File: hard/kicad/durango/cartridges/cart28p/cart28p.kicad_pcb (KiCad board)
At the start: 2 copper layers, 6 parts, among them J2 CARTRIDGE SLOT, U1 27C512

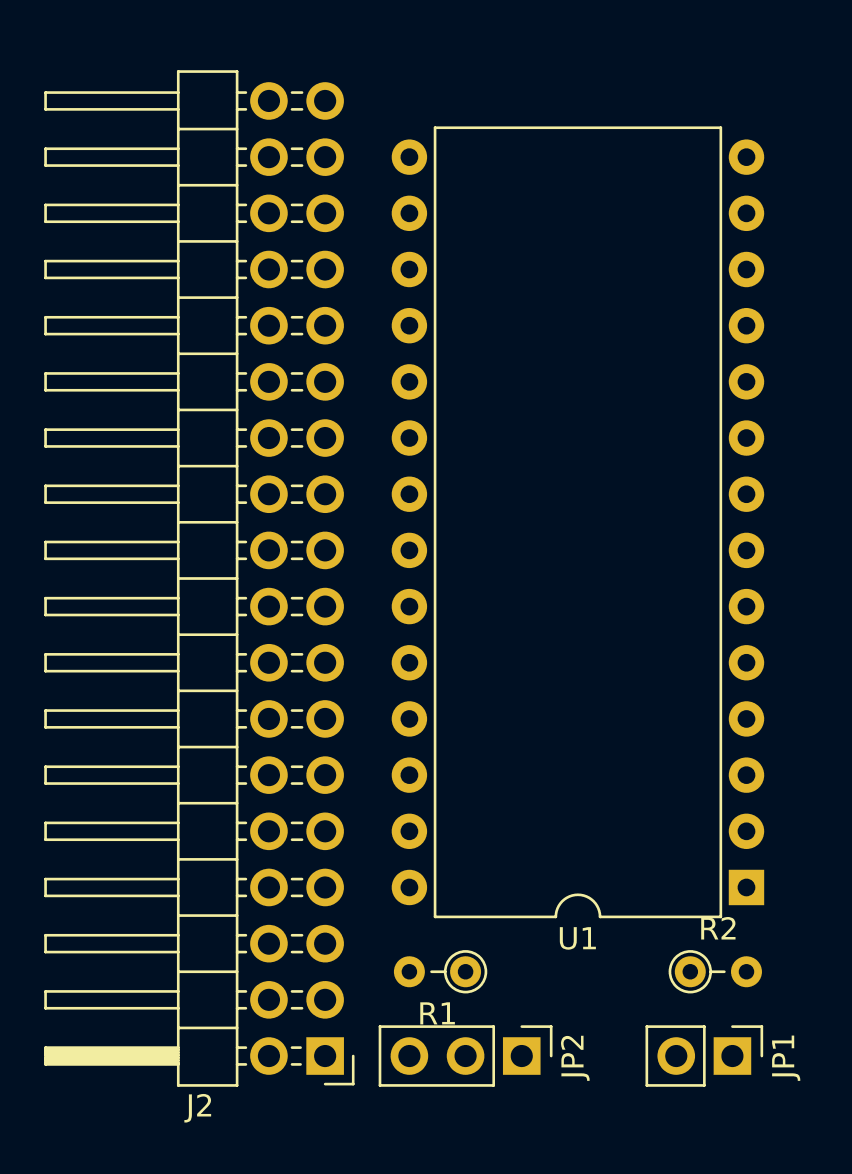
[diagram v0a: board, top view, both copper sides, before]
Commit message: fill 28p cartridge
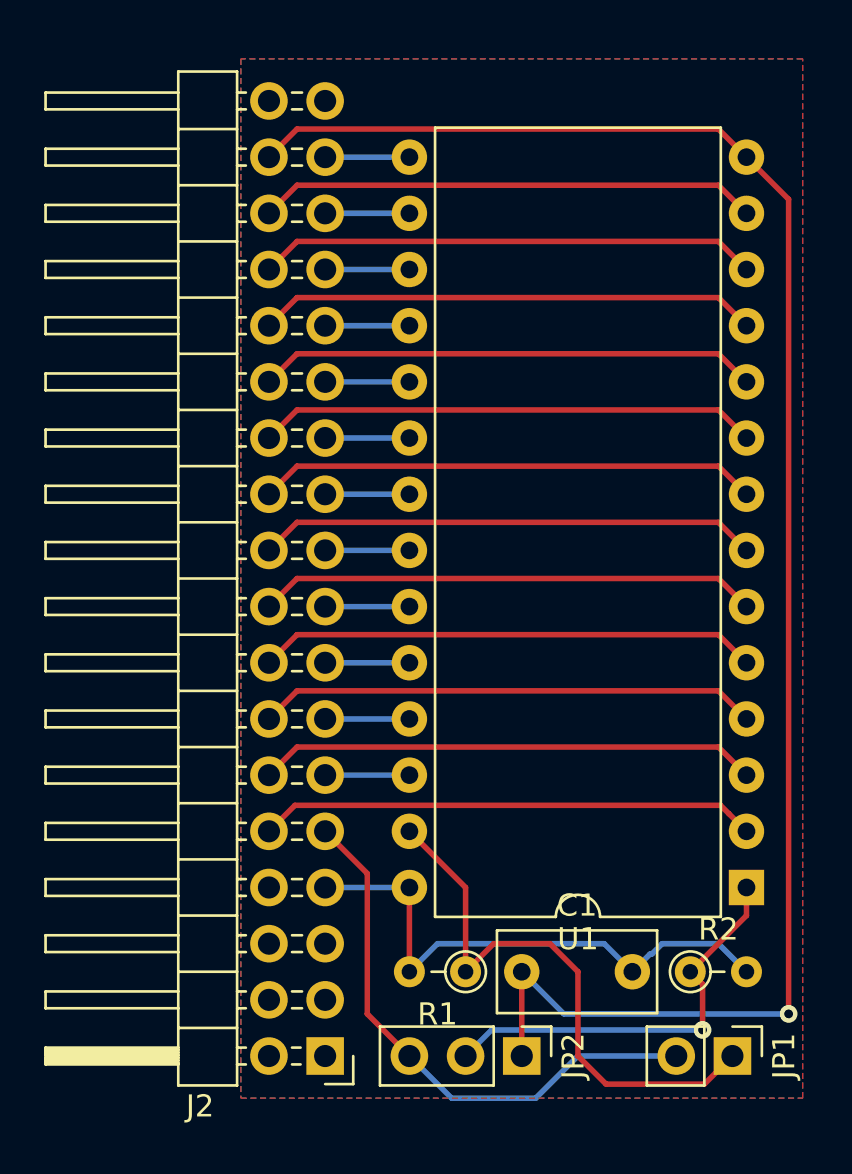
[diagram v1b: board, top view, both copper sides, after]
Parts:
- added C1: 100n, Capacitor_THT:C_Rect_L7.0mm_W3.5mm_P5.00mm, F.Cu at (71.8, 69.8)
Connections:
- net Net-(JP1-Pad1) renamed /A14_32+
- net Net-(JP2-Pad2) renamed /A15_F
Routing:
- net GND: track 0.00 -> 78.8 mm, vias 0 -> 1
- net /A14_32+: track 0.00 -> 25.4 mm
- net /A14: track 0.00 -> 25.4 mm
- net +5V: track 0.00 -> 25.0 mm
- net /D2: track 0.00 -> 22.6 mm
- net /D1: track 0.00 -> 22.6 mm
- net /D0: track 0.00 -> 22.6 mm
- net /A7: track 0.00 -> 22.6 mm
- net /A6: track 0.00 -> 22.6 mm
- net /A5: track 0.00 -> 22.6 mm
- net /A4: track 0.00 -> 22.6 mm
- net /A0: track 0.00 -> 22.6 mm
- net /A3: track 0.00 -> 22.6 mm
- net /A2: track 0.00 -> 22.6 mm
- net /A1: track 0.00 -> 22.6 mm
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- added copper zone on B.Cu, net +5V
- added copper zone on F.Cu, net GND

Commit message: add cartridge edge connector
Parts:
- removed J2: CARTRIDGE SLOT, Connector_PinHeader_2.54mm:PinHeader_2x18_P2.54mm_Horizontal
- added J1: Edge Connector, edge_conn:Durango_ROM, F.Cu at (55.9, 27.9)
- moved R2 2.54 mm to (81.9, 69.8), turned to 180 degrees
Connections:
- net /A15_F renamed /A15
- JP1 pad 1: /A14_32+ -> /A14
- JP1 pad 2: /A14 -> /CA14
- JP2 pad 3: /A14 -> /CA14
- R1 pad 1: /A14_32+ -> /A14
- U1 pad 27: /A14_32+ -> /A14
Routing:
- net /CA14: track 0.00 -> 31.3 mm
- net /A14_32+: track 25.4 -> 0.00 mm
- net GND: track 78.8 -> 73.3 mm, vias 1 -> 0
- net /~OE: track 3.81 -> 6.98 mm
- net /~CS: track 3.81 -> 6.98 mm
- net /D7: track 3.81 -> 6.98 mm
- net /D6: track 3.81 -> 6.98 mm
- net /D5: track 3.81 -> 6.98 mm
- net /D4: track 3.81 -> 6.98 mm
- net /D3: track 3.81 -> 6.98 mm
- net /A9: track 3.81 -> 6.98 mm
- net /A8: track 3.81 -> 6.98 mm
- net /A13: track 3.81 -> 6.98 mm
- net /A11: track 3.81 -> 6.98 mm
- net /A10: track 3.81 -> 6.98 mm
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- added copper zone on F.Cu, net +5V
- added copper zone on B.Cu, net GND
- removed copper zone on B.Cu, net +5V
- removed copper zone on F.Cu, net GND
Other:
- board outline added: 27.9 x 48.3 mm
- net class POWER added: clearance 0.25, trace_width 0.4, via_dia 0.8, via_drill 0.4

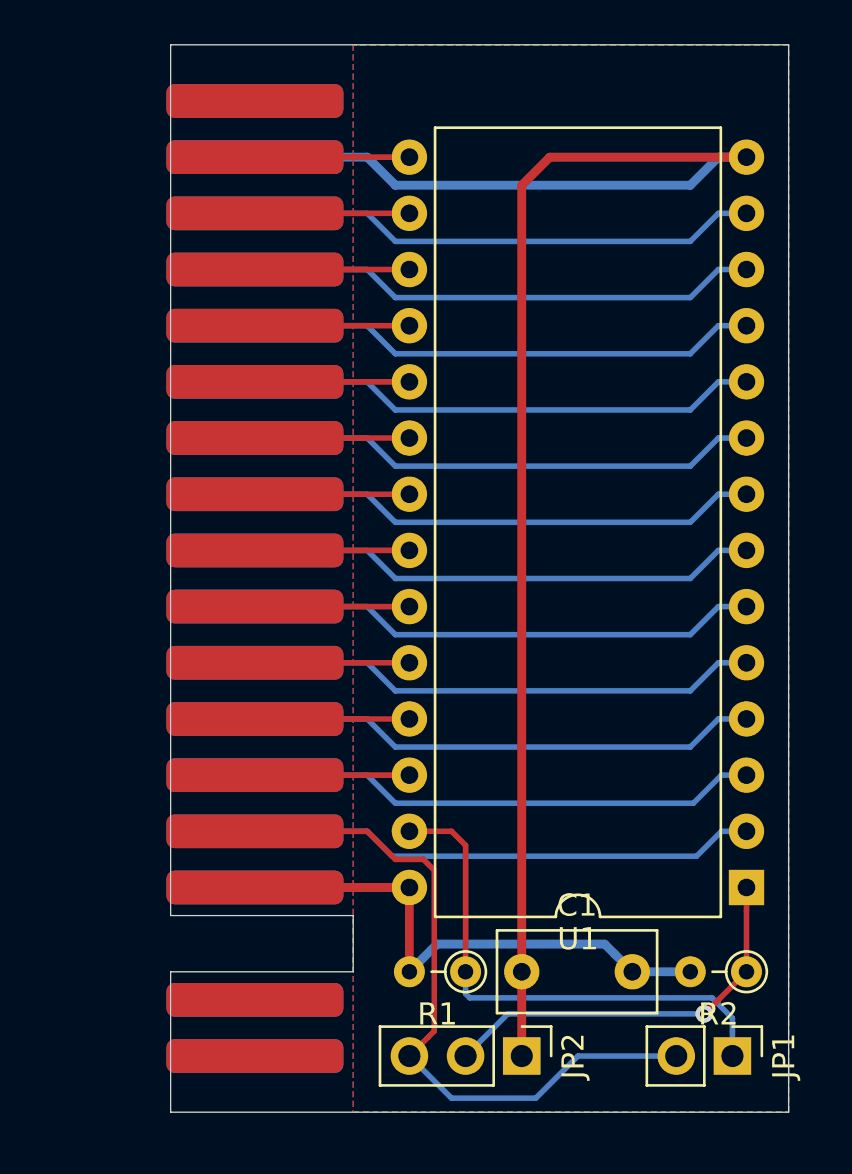
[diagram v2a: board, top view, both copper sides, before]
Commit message: improve 28p cartridge design
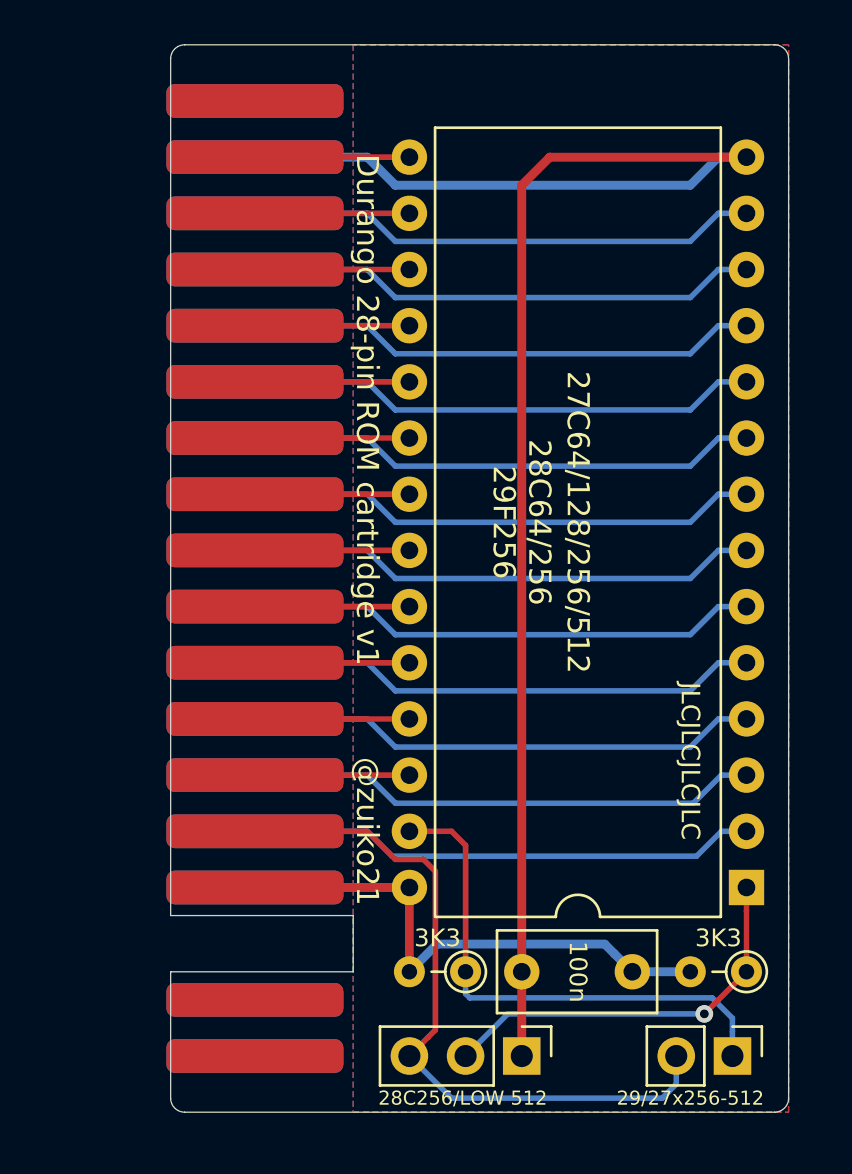
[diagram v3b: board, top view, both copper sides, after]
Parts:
- JP1: value 27x256-512 -> 29/27x256-512
- JP2: value LOW 512/28C256 -> 28C256/LOW 512
- U1: value 27C512 -> 27C64/128/256/512
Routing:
- net /CA14: track 31.3 -> 32.1 mm
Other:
- outline, holes or cut-outs redrawn
- board text added: "28C64/256 29F256"
- board text added: "@zuiko21"
- board text added: "Durango 28-pin ROM cartridge v1"
- board text added: "JLCJLCJLCJLC"

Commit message: add wrong gerbers for 28p cart
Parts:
- JP1: value 29/27x256-512 -> 27/29-32K+
- JP2: value 28C256/LOW 512 -> 28C/L32
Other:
- outline, holes or cut-outs redrawn
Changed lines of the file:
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@@
   (general
     (thickness 1.6)
-    (drawings 17)
+    (drawings 16)
     (tracks 115)
     (zones 0)
@@
   (page A4)
   (layers
-    (0 F.Cu signal)
-    (31 B.Cu signal)
-    (32 B.Adhes user)
-    (33 F.Adhes user)
-    (34 B.Paste user)
-    (35 F.Paste user)
-    (36 B.SilkS user)
-    (37 F.SilkS user)
-    (38 B.Mask user)
-    (39 F.Mask user)
-    (40 Dwgs.User user)
-    (41 Cmts.User user)
-    (42 Eco1.User user)
-    (43 Eco2.User user)
+    (0 F.Cu signal hide)
+    (31 B.Cu signal hide)
+    (32 B.Adhes user hide)
+    (33 F.Adhes user hide)
+    (34 B.Paste user hide)
+    (35 F.Paste user hide)
+    (36 B.SilkS user hide)
+    (37 F.SilkS user hide)
+    (38 B.Mask user hide)
+    (39 F.Mask user hide)
+    (40 Dwgs.User user hide)
+    (41 Cmts.User user hide)
+    (42 Eco1.User user hide)
+    (43 Eco2.User user hide)
     (44 Edge.Cuts user)
-    (45 Margin user)
-    (46 B.CrtYd user)
-    (47 F.CrtYd user)
-    (48 B.Fab user)
-    (49 F.Fab user)
+    (45 Margin user hide)
+    (46 B.CrtYd user hide)
+    (47 F.CrtYd user hide)
+    (48 B.Fab user hide)
+    (49 F.Fab user hide)
   )
   (setup
@@
     (pcbplotparams
       (layerselection 0x010fc_ffffffff)
-      (usegerberextensions false)
+      (usegerberextensions true)
       (usegerberattributes false)
       (usegerberadvancedattributes false)
       (creategerberjobfile false)
       (excludeedgelayer true)
-      (linewidth 0.100000)
+      (linewidth 0.150000)
       (plotframeref false)
       (viasonmask false)
@@
       (plotinvisibletext false)
       (padsonsilk false)
-      (subtractmaskfromsilk false)
+      (subtractmaskfromsilk true)
       (outputformat 1)
       (mirror false)
-      (drillshape 1)
+      (drillshape 0)
       (scaleselection 1)
-      (outputdirectory ""))
+      (outputdirectory "gerber/"))
   )
   (net 0 "")
@@
     (at 55.88 27.94 270)
     (fp_text reference J1 (at 2.54 -8.89 unlocked) (layer B.SilkS)
-      (effects (font (size 1 1) (thickness 0.15)) (justify mirror))
+      (effects (font (size 1.016 1.016) (thickness 0.16)) (justify mirror))
     )
     (fp_text value "Edge Connector" (at 24.13 1.27 90) (layer F.Fab)
@@
     (tags "THT DIP DIL PDIP 2.54mm 15.24mm 600mil")
     (fp_text reference U1 (at 7.493 16.51 unlocked) (layer B.SilkS)
-      (effects (font (size 1 1) (thickness 0.15)) (justify mirror))
+      (effects (font (size 1.016 1.016) (thickness 0.16)) (justify mirror))
     )
     (fp_text value 27C64/128/256/512 (at 7.62 16.51 270 unlocked) (layer F.SilkS)
-      (effects (font (size 1 1) (thickness 0.15)))
+      (effects (font (size 1.016 1.016) (thickness 0.16)))
     )
     (fp_arc (start 7.62 -1.33) (end 6.62 -1.33) (angle -180) (layer F.SilkS) (width 0.12))
@@
     (tags "C Rect series Radial pin pitch 5.00mm  length 7mm width 3.5mm Capacitor")
     (fp_text reference C1 (at 2.5 0) (layer B.SilkS)
-      (effects (font (size 1 1) (thickness 0.15)) (justify mirror))
+      (effects (font (size 1 1) (thickness 0.16)) (justify mirror))
     )
     (fp_text value 100n (at 2.54 0 270 unlocked) (layer F.SilkS)
-      (effects (font (size 0.8 0.8) (thickness 0.12)))
+      (effects (font (size 1.016 1.016) (thickness 0.16)))
     )
     (fp_text user %R (at 2.5 0) (layer F.Fab)
-      (effects (font (size 1 1) (thickness 0.15)))
+      (effects (font (size 1 1) (thickness 0.16)))
     )
     (fp_line (start 6.25 -2) (end -1.25 -2) (layer F.CrtYd) (width 0.05))
@@
     (tags "Resistor Axial_DIN0204 series Axial Vertical pin pitch 2.54mm 0.167W length 3.6mm diameter 1.6mm")
     (fp_text reference R2 (at 1.27 1.524 unlocked) (layer B.SilkS)
-      (effects (font (size 1 1) (thickness 0.15)) (justify mirror))
+      (effects (font (size 1.016 1.016) (thickness 0.16)) (justify mirror))
     )
     (fp_text value 3K3 (at 1.27 1.524 unlocked) (layer F.SilkS)
-      (effects (font (size 0.8 0.8) (thickness 0.12)))
+      (effects (font (size 1.016 1.016) (thickness 0.16)))
     )
     (fp_text user %R (at 1.27 -1.92) (layer F.Fab)
@@
     (tags "Resistor Axial_DIN0204 series Axial Vertical pin pitch 2.54mm 0.167W length 3.6mm diameter 1.6mm")
     (fp_text reference R1 (at 1.27 1.524) (layer B.SilkS)
-      (effects (font (size 1 1) (thickness 0.15)) (justify mirror))
+      (effects (font (size 1.016 1.016) (thickness 0.16)) (justify mirror))
     )
     (fp_text value 3K3 (at 1.27 1.524 unlocked) (layer F.SilkS)
-      (effects (font (size 0.8 0.8) (thickness 0.12)))
+      (effects (font (size 1.016 1.016) (thickness 0.16)))
     )
     (fp_text user %R (at 1.27 -1.92) (layer F.Fab)
@@
     (tags "Through hole pin header THT 1x03 2.54mm single row")
     (fp_text reference JP2 (at -1.778 2.413 unlocked) (layer B.SilkS)
-      (effects (font (size 1 1) (thickness 0.15)) (justify mirror))
-    )
-    (fp_text value "28C256/LOW 512" (at 1.905 2.667 unlocked) (layer F.SilkS)
-      (effects (font (size 0.635 0.635) (thickness 0.1)))
+      (effects (font (size 1.016 1.016) (thickness 0.16)) (justify mirror))
+    )
+    (fp_text value 28C/L32 (at 1.905 2.667 unlocked) (layer F.SilkS)
+      (effects (font (size 1.016 1.016) (thickness 0.153)))
     )
     (fp_text user %R (at 0 2.54) (layer F.Fab)
@@
     (tags "Through hole pin header THT 1x02 2.54mm single row")
     (fp_text reference JP1 (at -1.778 1.27 unlocked) (layer B.SilkS)
-      (effects (font (size 1 1) (thickness 0.15)) (justify mirror))
-    )
-    (fp_text value 29/27x256-512 (at 1.905 1.905 unlocked) (layer F.SilkS)
-      (effects (font (size 0.635 0.635) (thickness 0.1)))
+      (effects (font (size 1.016 1.016) (thickness 0.16)) (justify mirror))
+    )
+    (fp_text value 27/29-32K+ (at 1.905 2.54 unlocked) (layer F.SilkS)
+      (effects (font (size 1.016 1.016) (thickness 0.153)))
     )
     (fp_text user %R (at 0 1.27) (layer F.Fab)
@@
   )
   (gr_text "28C64/256\n29F256" (at 71.755 49.53 270) (layer F.SilkS)
-    (effects (font (size 1 1) (thickness 0.15)))
+    (effects (font (size 1.016 1.016) (thickness 0.16)))
   )
   (gr_text JLCJLCJLCJLC (at 79.375 60.325 270) (layer F.SilkS)
-    (effects (font (size 0.84 0.84) (thickness 0.1575)))
+    (effects (font (size 1.016 1.016) (thickness 0.1575)))
   )
   (gr_arc (start 83.185 75.565) (end 83.185 76.2) (angle -90) (layer Edge.Cuts) (width 0.05))
   (gr_arc (start 56.515 75.565) (end 55.88 75.565) (angle -90) (layer Edge.Cuts) (width 0.05))
-  (gr_arc (start 56.515 28.575) (end 56.515 27.94) (angle -90) (layer Edge.Cuts) (width 0.05))
   (gr_arc (start 56.515 28.575) (end 56.515 27.94) (angle 0) (layer Edge.Cuts) (width 0.05))
   (gr_arc (start 83.185 28.575) (end 83.82 28.575) (angle -90) (layer Edge.Cuts) (width 0.05))
   (gr_text @zuiko21 (at 64.77 63.5 270) (layer F.SilkS)
-    (effects (font (size 1 1) (thickness 0.18)))
+    (effects (font (size 1.016 1.016) (thickness 0.18)))
   )
   (gr_text "Durango 28-pin ROM cartridge v1" (at 64.77 44.45 270) (layer F.SilkS)
-    (effects (font (size 1 1) (thickness 0.15)))
+    (effects (font (size 1.016 1.016) (thickness 0.16)))
   )
   (gr_line (start 55.88 69.85) (end 55.88 75.565) (layer Edge.Cuts) (width 0.05))
@@
   (gr_line (start 64.135 67.31) (end 64.135 69.85) (layer Edge.Cuts) (width 0.05))
   (gr_line (start 55.88 67.31) (end 64.135 67.31) (layer Edge.Cuts) (width 0.05))
-  (gr_line (start 55.88 28.575) (end 55.88 67.31) (layer Edge.Cuts) (width 0.05))
-  (gr_line (start 83.185 27.94) (end 56.515 27.94) (layer Edge.Cuts) (width 0.05))
+  (gr_line (start 55.88 27.94) (end 55.88 67.31) (layer Edge.Cuts) (width 0.05))
+  (gr_line (start 83.185 27.94) (end 55.88 27.94) (layer Edge.Cuts) (width 0.05))
   (gr_line (start 83.82 75.565) (end 83.82 28.575) (layer Edge.Cuts) (width 0.05))
   (gr_line (start 56.515 76.2) (end 83.185 76.2) (layer Edge.Cuts) (width 0.05))
